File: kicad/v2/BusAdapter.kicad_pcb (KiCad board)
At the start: 2 copper layers, 99.1 x 99.1 mm, 55 parts, among them J1 Conn_02x17_Odd_Even, J10 Conn_02x06_Odd_Even, J11 Conn_02x02_Odd_Even, J12 Conn_02x06_Top_Bottom, J13 Conn_01x03, J14 Conn_01x02, J2 Conn_02x20_Odd_Even, J3 Conn_02x20_Odd_Even, J4 Conn_02x06_Top_Bottom, J5 Conn_02x06_Top_Bottom, J6 Conn_Coaxial, J7 Conn_Coaxial, J8 Conn_01x02_Male, J9 Conn_01x02_Male, Q1 2N3904, Q2 2N3904, SW1 SW_Push, SW2 SW_Push, U1 74LVC245, U2 74LVC245, U3 74LVC245, U4 IS61C5128AL-10TLI, U5 MCP4822

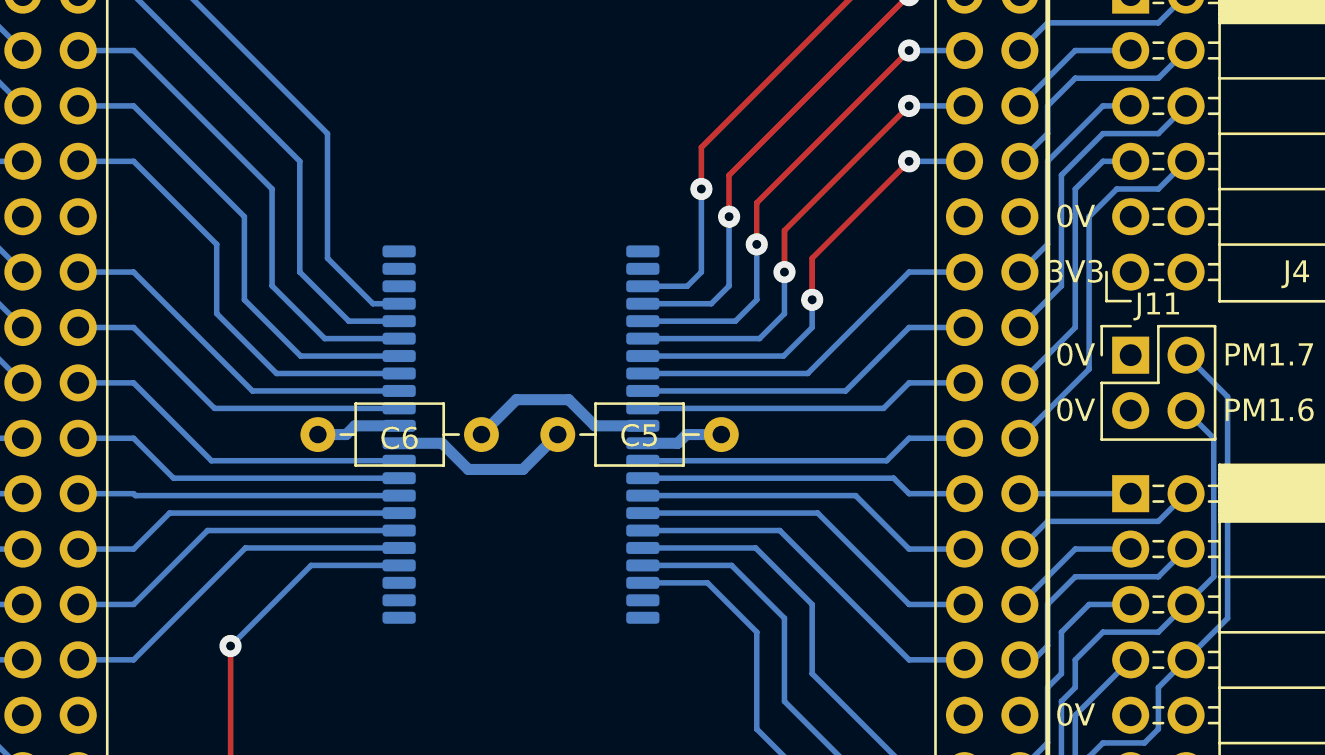
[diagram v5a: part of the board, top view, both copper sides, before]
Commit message: PCB v2: Made TSOP-II pads 0.5mm longer on the outside
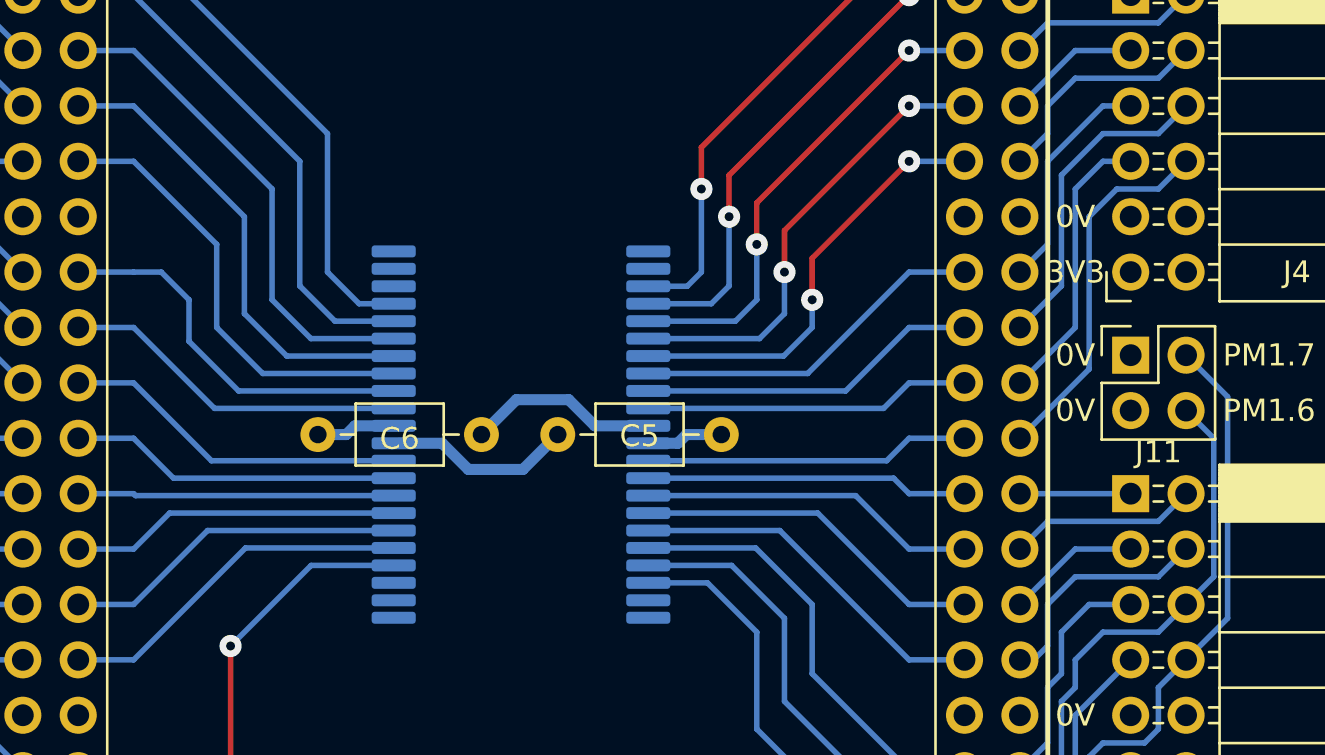
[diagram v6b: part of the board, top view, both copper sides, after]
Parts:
- U4: footprint Package_SO:TSOP-II-44_10.16x18.41mm_P0.8mm -> footprints:TSOP-II-44_10.16x18.41mm_P0.8mm
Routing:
- net /RAMD7: track 17.0 -> 18.1 mm
